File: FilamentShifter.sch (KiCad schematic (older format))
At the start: 4 parts

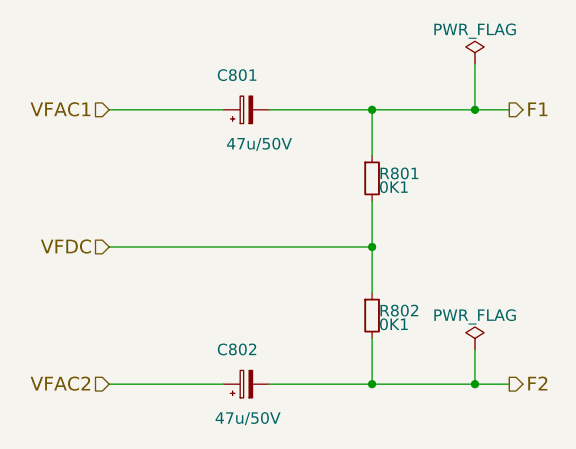
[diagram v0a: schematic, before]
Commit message: switching to more convenient notation of values, e.g. 100K instead of 0M1
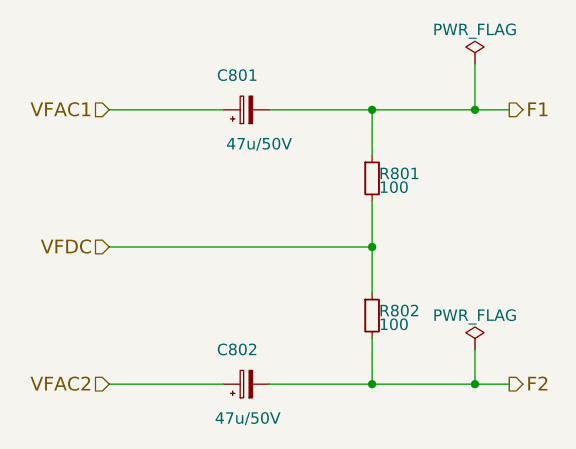
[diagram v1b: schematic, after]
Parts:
- R501, R502: value 0K1 -> 100
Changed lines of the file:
@@
 AR Path="/5AAC050F/5AAC05F0/5AAC08BA/5AAAF458" Ref="R801"  Part="1"
 F 0 "R801" H 2630 2420 50  0000 L CNN
-F 1 "0K1" H 2630 2360 50  0000 L CNN
+F 1 "100" H 2630 2360 50  0000 L CNN
 F 2 "Resistors_SMD:R_0805_HandSoldering" H 2600 2400 50  0001 C CNN
 F 3 "" H 2600 2400 50  0001 C CNN
@@
 AR Path="/5AAC050F/5AAC05F0/5AAC08BA/5AAAF487" Ref="R802"  Part="1"
 F 0 "R802" H 2630 3020 50  0000 L CNN
-F 1 "0K1" H 2630 2960 50  0000 L CNN
+F 1 "100" H 2630 2960 50  0000 L CNN
 F 2 "Resistors_SMD:R_0805_HandSoldering" H 2600 3000 50  0001 C CNN
 F 3 "" H 2600 3000 50  0001 C CNN
